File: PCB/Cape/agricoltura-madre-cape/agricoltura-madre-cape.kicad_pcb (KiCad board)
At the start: 2 copper layers, 54.6 x 86.4 mm, 2 parts, among them P8 BeagleBone_Black_Header, P9 BeagleBone_Black_Header

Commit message: Datasheets and BBG version
Finished initial schematic for BBG Gateway version and added datasheets for ST sub 1GHZ RF hardware.
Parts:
- added C1: C0402C104K9PACTU, AVR-KiCAD-Lib-Resistors:R0402, F.Cu at (95.9, 109.5)
- added C2: C0402C104K9PACTU, AVR-KiCAD-Lib-Resistors:R0402, F.Cu at (77.2, 122.9)
- added C3: CGA3E2X7R1H104K080AA, AVR-KiCAD-Lib-Capacitors:C0603, F.Cu at (63.4, 128.2)
- added C4: CGA3E2X7R1H104K080AA, AVR-KiCAD-Lib-Capacitors:C0603, F.Cu at (59.8, 128.2)
- added C5: C0402C104K9PACTU, AVR-KiCAD-Lib-Resistors:R0402, F.Cu at (333.6, 65.2)
- added D1: LTST-C194TBKT, AVR-KiCAD-Lib-Diodes:LED0603, F.Cu at (333.7, 61.0)
- added M1: SPSGRFC-915, AVR-KiCAD-Lib-Modules:XCVR_SPSGRF-915, F.Cu at (323.8, 68.6)
- added R1: RC0402FR-0733RL, AVR-KiCAD-Lib-Resistors:R0402, F.Cu at (199.7, 121.4)
- added R10: RC0402FR-071KL, AVR-KiCAD-Lib-Resistors:R0402, F.Cu at (77.2, 120.9)
- added R11: RC0402FR-071KL, AVR-KiCAD-Lib-Resistors:R0402, F.Cu at (66.7, 128.0)
- added R12: RC0402FR-0710KL, AVR-KiCAD-Lib-Resistors:R0402, F.Cu at (333.6, 63.1)
- added R13: RC0402FR-071KL, AVR-KiCAD-Lib-Resistors:R0402, F.Cu at (337.1, 60.9)
- added R2: RC0402FR-0733RL, AVR-KiCAD-Lib-Resistors:R0402, F.Cu at (213.9, 60.9)
- added R3: RC0402FR-0733RL, AVR-KiCAD-Lib-Resistors:R0402, F.Cu at (202.7, 121.4)
- added R4: RC0402FR-0733RL, AVR-KiCAD-Lib-Resistors:R0402, F.Cu at (216.9, 60.9)
- added R5: RC0402FR-0733RL, AVR-KiCAD-Lib-Resistors:R0402, F.Cu at (213.9, 63.0)
- added R6: RC0402FR-071KL, AVR-KiCAD-Lib-Resistors:R0402, F.Cu at (80.2, 120.9)
- added R7: RC0402FR-071KL, AVR-KiCAD-Lib-Resistors:R0402, F.Cu at (72.6, 128.0)
- added R8: RC0402FR-071KL, AVR-KiCAD-Lib-Resistors:R0402, F.Cu at (95.9, 111.5)
- added R9: RC0402FR-071KL, AVR-KiCAD-Lib-Resistors:R0402, F.Cu at (69.7, 128.0)
- added T1: 0395121004, AVR-KiCAD-Lib-Connectors:0395121004, F.Cu at (77.1, 108.4)
- added T2: 0395121004, AVR-KiCAD-Lib-Connectors:0395121004, F.Cu at (58.9, 108.4)
- added U1: MAX13450EAUD+, AVR-KiCAD-Lib-ICs:MAX13450EAUD&plus_, F.Cu at (71.3, 123.6)
- added U2: MAX13450EAUD+, AVR-KiCAD-Lib-ICs:MAX13450EAUD&plus_, F.Cu at (62.4, 123.6)
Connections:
- net GNDD renamed GND
- P9 pad 11: Net-(P9-Pad11) -> /Beaglebone Interface/RS485_UART_RX1
- P9 pad 12: Net-(P9-Pad12) -> /Beaglebone Interface/RS485_DE1
- P9 pad 13: Net-(P9-Pad13) -> /Beaglebone Interface/RS485_UART_TX1
- P9 pad 14: Net-(P9-Pad14) -> /Beaglebone Interface/RS485_RE1
- P9 pad 16: Net-(P9-Pad16) -> /Beaglebone Interface/RS485_TERM_EN1
- P9 pad 17: Net-(P9-Pad17) -> /Beaglebone Interface/SPI0_CS0
- P9 pad 18: Net-(P9-Pad18) -> /Beaglebone Interface/SPI0_D1
- P9 pad 20: Net-(P9-Pad20) -> /Beaglebone Interface/RS485_SL_RATE1
- P9 pad 21: Net-(P9-Pad21) -> /Beaglebone Interface/SPI0_D0
- P9 pad 22: Net-(P9-Pad22) -> /Beaglebone Interface/SPI0_SCLK
- P9 pad 23: Net-(P9-Pad23) -> /Beaglebone Interface/RS485_DE2
- P9 pad 24: Net-(P9-Pad24) -> /Beaglebone Interface/RS485_UART_TX2
- P9 pad 25: Net-(P9-Pad25) -> /Beaglebone Interface/RS485_RE2
- P9 pad 26: Net-(P9-Pad26) -> /Beaglebone Interface/RS485_UART_RX2
- P9 pad 27: Net-(P9-Pad27) -> /Beaglebone Interface/RS485_SL_RATE2
- P9 pad 29: Net-(P9-Pad29) -> /Beaglebone Interface/RS485_TERM_EN2

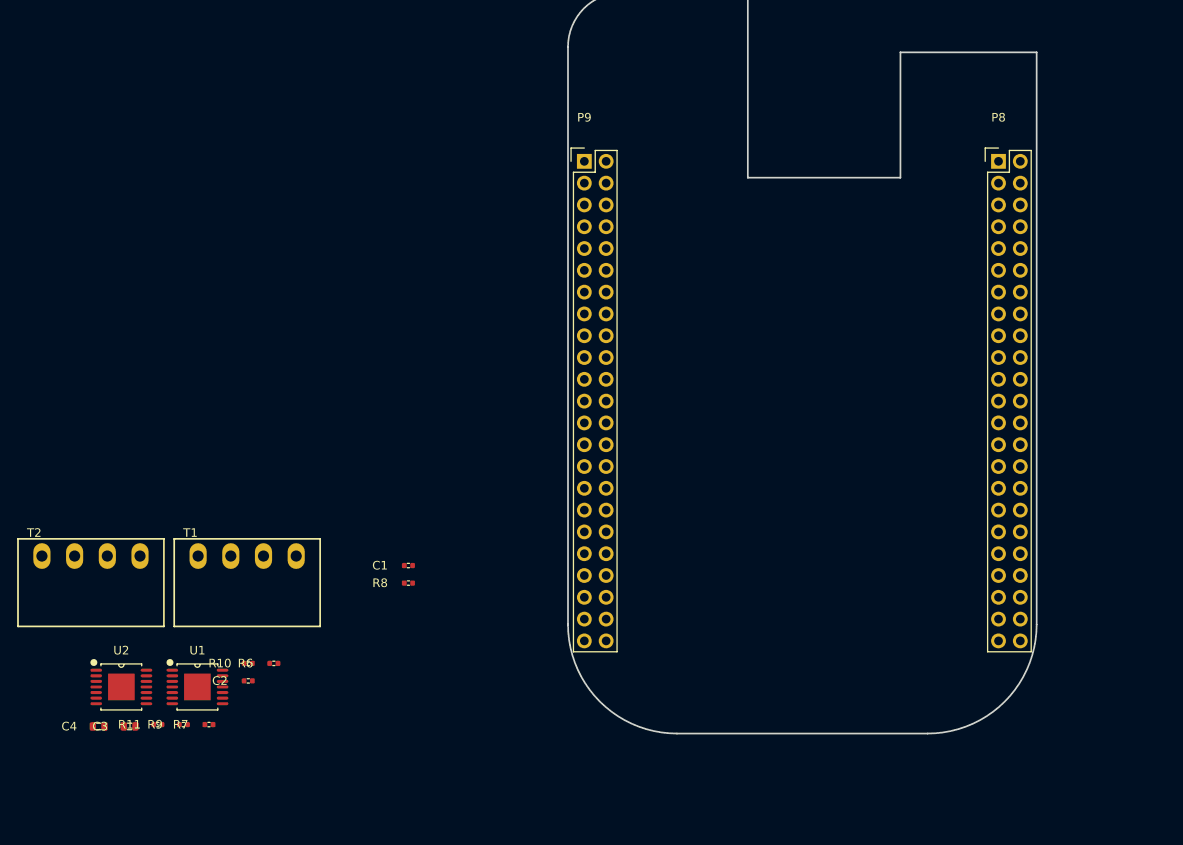
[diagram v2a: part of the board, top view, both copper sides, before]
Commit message: Board Work
Board shape added working on cut outs
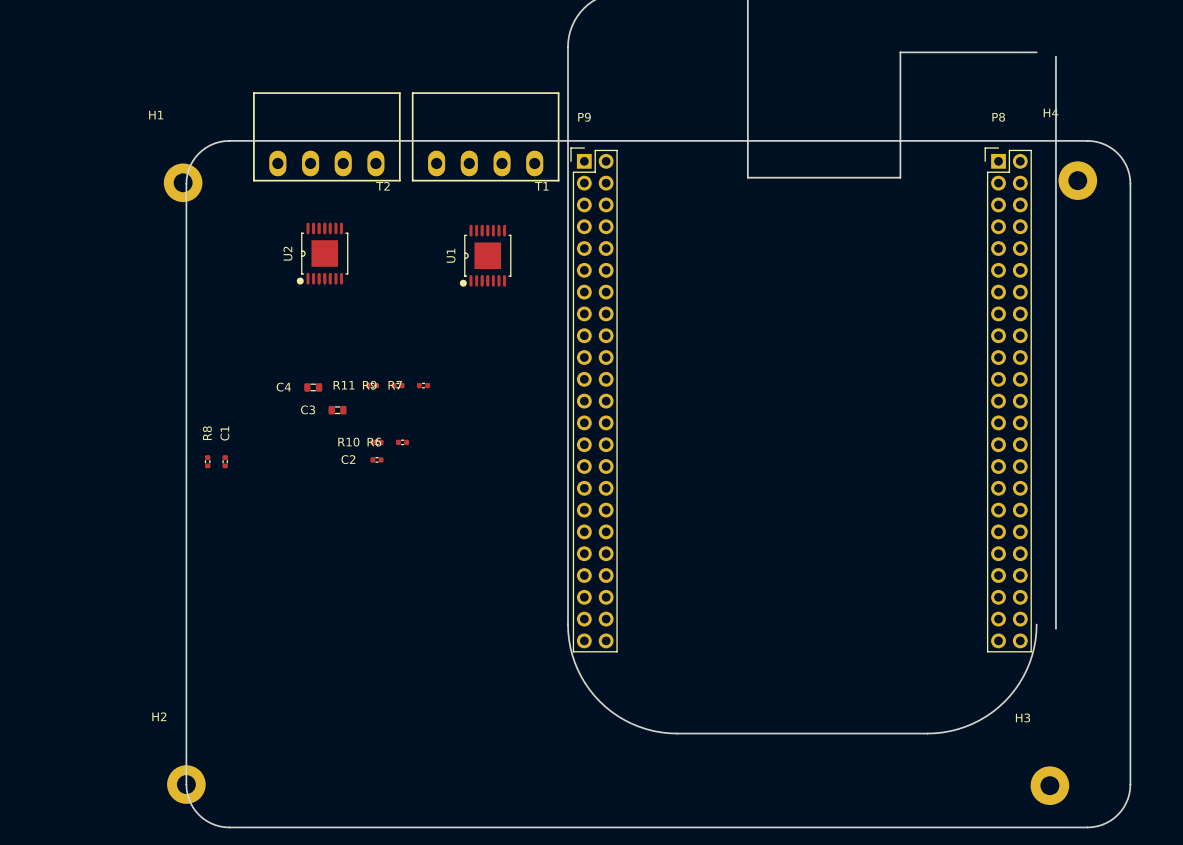
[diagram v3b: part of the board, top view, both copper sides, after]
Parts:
- added H1: M2_Plated_Hole, AVR-KiCAD-Lib-Holes_Fasteners:M2_HOLE, F.Cu at (69.6, 64.9)
- added H2: M2_Plated_Hole, AVR-KiCAD-Lib-Holes_Fasteners:M2_HOLE, F.Cu at (70.0, 135.0)
- added H3: M2_Plated_Hole, AVR-KiCAD-Lib-Holes_Fasteners:M2_HOLE, F.Cu at (170.6, 135.1)
- added H4: M2_Plated_Hole, AVR-KiCAD-Lib-Holes_Fasteners:M2_HOLE, F.Cu at (173.9, 64.6)
- moved U1 60.6 mm to (105.1, 73.4), turned to 90 degrees
- moved U2 55.8 mm to (86.1, 73.1), turned to 90 degrees
- moved T1 53.5 mm to (104.9, 62.6), turned to 180 degrees
- moved T2 53.4 mm to (86.4, 62.6), turned to 180 degrees
- moved R11 46.7 mm to (91.7, 88.5)
- moved R7 46.7 mm to (97.6, 88.5)
- moved R9 46.7 mm to (94.7, 88.5)
- moved C4 46.7 mm to (84.8, 88.7)
- moved C3 44.1 mm to (87.6, 91.4)
- moved C2 29.8 mm to (92.2, 97.2)
- moved R10 29.8 mm to (92.2, 95.1)
- moved R6 29.8 mm to (95.2, 95.1)
- moved R8 27.3 mm to (72.5, 97.4), turned to 270 degrees
- moved C1 24.5 mm to (74.5, 97.4), turned to 270 degrees
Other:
- board size 54.6 x 86.4 mm -> 110 x 97.3 mm
